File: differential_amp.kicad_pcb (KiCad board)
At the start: 2 copper layers, 36.8 x 56.8 mm, 29 parts, among them J1 RJ45, P1 CON, P2 gnd_ref, U1 AD8422, U2 AD8609

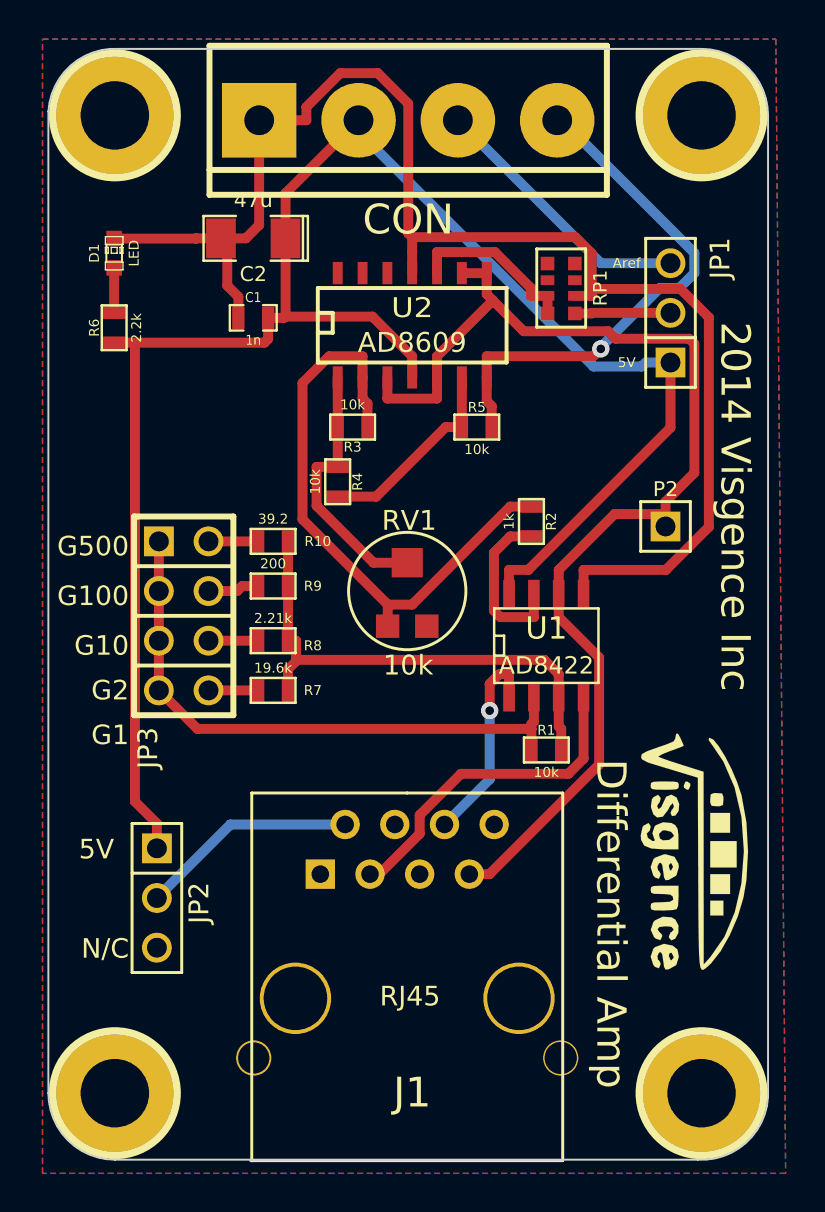
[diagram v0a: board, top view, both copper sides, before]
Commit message: Removed rj45, added multiturn pot
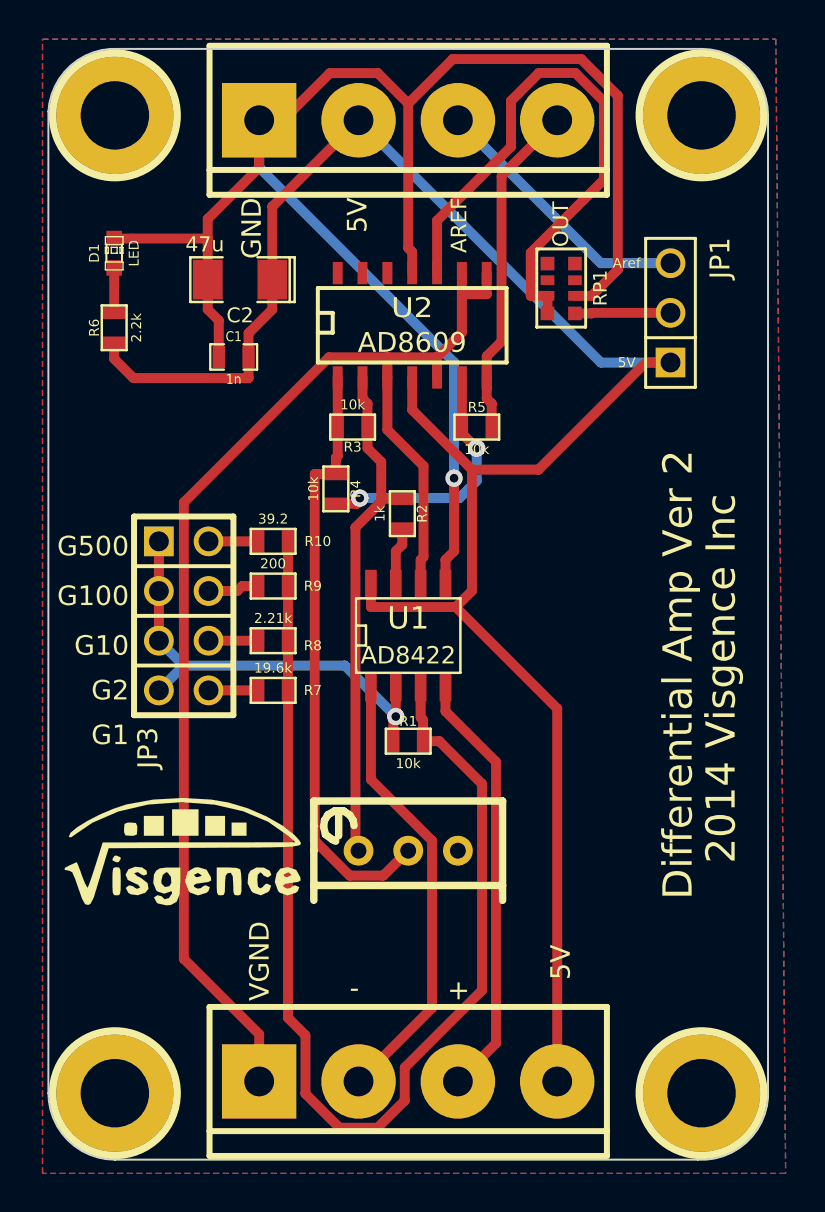
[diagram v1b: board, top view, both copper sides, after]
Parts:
- removed the G*** at (71.9, 75.2)
- removed J1: RJ45, RJ45_8_ASSMAN
- removed JP2: PWR, PIN_ARRAY_3X1
- removed P2: gnd_ref, PIN_ARRAY_1
- added G1: LOGO, visgence_parts:LOGO, F.Cu at (45.8, 75.0)
- added P3: CONN_4, Connect:bornier4, F.Cu at (57.2, 86.8)
- D1: footprint LED-0603 -> LEDs:LED-0603
- P1: footprint bornier4 -> Connect:bornier4
- RV1: footprint TC33X-2 -> Potentiometers:Potentiometer_Bourns_3296W_3-8Zoll_Inline_ScrewUp
- moved RV1 13.3 mm to (57.2, 75.0), turned to 270 degrees
- moved U1 7.08 mm to (57.2, 64.0)
- moved R1 7.08 mm to (57.2, 69.4)
- moved R2 6.61 mm to (56.9, 57.8)
- moved C1 2.24 mm to (48.3, 49.8)
- moved C2 2.22 mm to (48.6, 45.8)
- moved R4 0.38 mm to (53.5, 56.5)
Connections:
- RP1 pad 3: (no net) -> Net-(RP1-Pad3)
- RP1 pad 4: (no net) -> Net-(RP1-Pad4)
- RP1 pad 5: (no net) -> Net-(RP1-Pad5)
- RP1 pad 6: (no net) -> Net-(RP1-Pad6)
- RV1 pad 3: (no net) -> Net-(RV1-Pad3)
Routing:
- net Net-(R1-Pad2): track 25.9 -> 59.5 mm
- net Net-(RP1-Pad7): track 8.80 -> 29.6 mm
- net Net-(R3-Pad2): track 13.5 -> 30.9 mm
- net GND: track 74.2 -> 88.8 mm, vias 0 -> 1
- net Net-(P3-Pad2): track 10.6 -> 23.0 mm, vias 1 -> 0
- net N-0000017: track 11.2 -> 0.00 mm
- net out: track 27.0 -> 17.3 mm, vias 1 -> 0
- net +5V: track 93.6 -> 102.4 mm
- net vgnd: track 60.2 -> 67.8 mm
- net Net-(JP3-Pad1): track 30.2 -> 23.4 mm, vias 0 -> 1
- net Net-(R2-Pad2): track 8.61 -> 2.94 mm
- net Net-(P3-Pad3): track 17.0 -> 22.0 mm
- net Net-(R2-Pad1): track 31.0 -> 26.3 mm
- net Net-(R4-Pad2): track 10.4 -> 13.4 mm, vias 0 -> 2
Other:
- board text added: "+"
- board text added: "-"
- board text added: "AREF"
- board text added: "Differential Amp Ver 2"
- board text added: "GND"
- board text added: "OUT"
- board text added: "VGND"
- board text removed: "Differential Amp"
- board text removed: "N/C"
